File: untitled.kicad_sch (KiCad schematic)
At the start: 25 parts, among them U1 RP2040, X1 ASE-12.0MHz

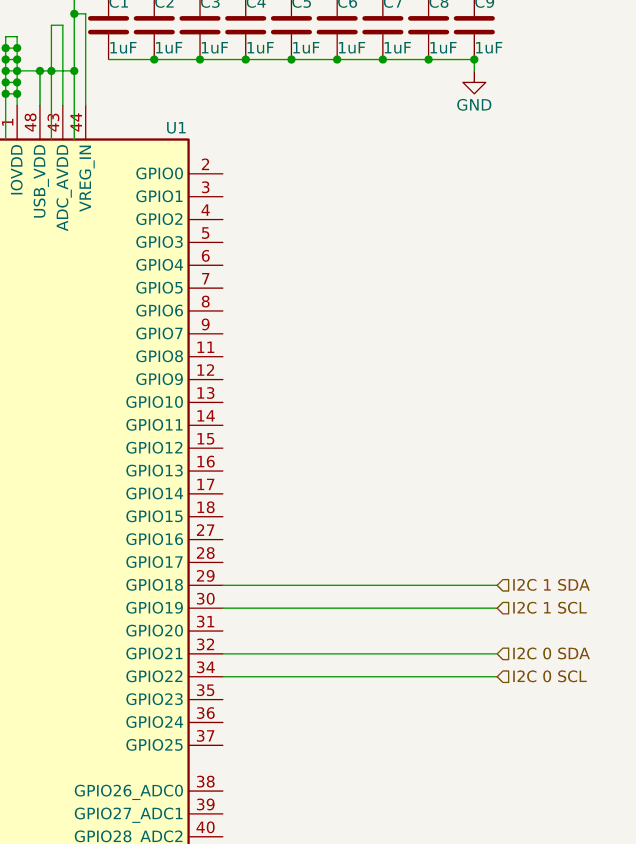
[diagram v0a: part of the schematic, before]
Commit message: exposes proper GPIO
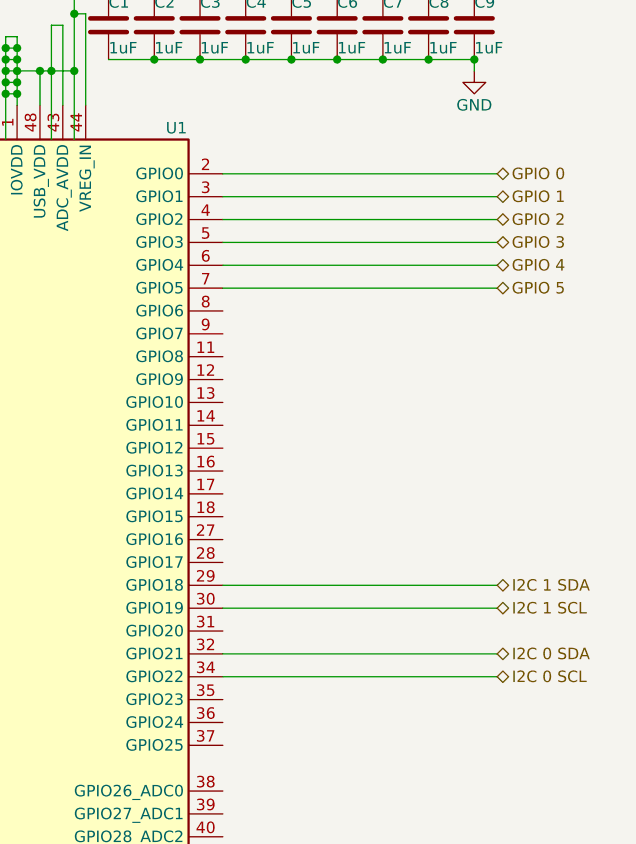
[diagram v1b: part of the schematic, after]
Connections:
- net GPIO 0: now reaches U1.2 (GPIO0)
- net GPIO 1: now reaches U1.3 (GPIO1)
- net GPIO 2: now reaches U1.4 (GPIO2)
- net GPIO 3: now reaches U1.5 (GPIO3)
- net GPIO 4: now reaches U1.6 (GPIO4)
- net GPIO 5: now reaches U1.7 (GPIO5)
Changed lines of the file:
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@@
+    (stroke (width 0) (type default))
+  )
+  (wire (pts (xy 143.51 52.07) (xy 173.99 52.07))
     (stroke (width 0) (type default))
   )
@@
     (stroke (width 0) (type default))
   )
+  (wire (pts (xy 143.51 46.99) (xy 173.99 46.99))
+    (stroke (width 0) (type default))
+  )
   (wire (pts (xy 125.73 34.29) (xy 125.73 25.4))
     (stroke (width 0) (type default))
@@
     (stroke (width 0) (type default))
   )
+  (wire (pts (xy 143.51 41.91) (xy 173.99 41.91))
+    (stroke (width 0) (type default))
+  )
   (wire (pts (xy 41.91 87.63) (xy 92.71 87.63))
     (stroke (width 0) (type default))
@@
     (stroke (width 0) (type default))
   )
+  (wire (pts (xy 143.51 49.53) (xy 173.99 49.53))
+    (stroke (width 0) (type default))
+  )
   (wire (pts (xy 120.65 30.48) (xy 120.65 29.21))
     (stroke (width 0) (type default))
@@
   )
   (wire (pts (xy 118.11 124.46) (xy 116.84 124.46))
+    (stroke (width 0) (type default))
+  )
+  (wire (pts (xy 143.51 54.61) (xy 173.99 54.61))
+    (stroke (width 0) (type default))
+  )
+  (wire (pts (xy 143.51 44.45) (xy 173.99 44.45))
     (stroke (width 0) (type default))
   )
@@
     (effects (font (size 1.27 1.27)) (justify left bottom))
   )
-  (hierarchical_label "I2C 1 SDA" (shape input) (at 173.99 87.63 0) (fields_autoplaced)
+  (hierarchical_label "I2C 1 SDA" (shape bidirectional) (at 173.99 87.63 0) (fields_autoplaced)
+    (effects (font (size 1.27 1.27)) (justify left))
+  )
+  (hierarchical_label "GPIO 5" (shape bidirectional) (at 173.99 54.61 0) (fields_autoplaced)
     (effects (font (size 1.27 1.27)) (justify left))
   )
@@
     (effects (font (size 1.27 1.27)) (justify right))
   )
+  (hierarchical_label "GPIO 4" (shape bidirectional) (at 173.99 52.07 0) (fields_autoplaced)
+    (effects (font (size 1.27 1.27)) (justify left))
+  )
   (hierarchical_label "USB_D-" (shape bidirectional) (at 74.93 49.53 180) (fields_autoplaced)
     (effects (font (size 1.27 1.27)) (justify right))
   )
+  (hierarchical_label "GPIO 2" (shape bidirectional) (at 173.99 46.99 0) (fields_autoplaced)
+    (effects (font (size 1.27 1.27)) (justify left))
+  )
+  (hierarchical_label "GPIO 0" (shape bidirectional) (at 173.99 41.91 0) (fields_autoplaced)
+    (effects (font (size 1.27 1.27)) (justify left))
+  )
   (hierarchical_label "QSPI_2" (shape bidirectional) (at 71.12 69.85 180) (fields_autoplaced)
     (effects (font (size 1.27 1.27)) (justify right))
@@
     (effects (font (size 1.27 1.27)) (justify left))
   )
-  (hierarchical_label "I2C 0 SDA" (shape input) (at 173.99 95.25 0) (fields_autoplaced)
+  (hierarchical_label "I2C 0 SDA" (shape bidirectional) (at 173.99 95.25 0) (fields_autoplaced)
     (effects (font (size 1.27 1.27)) (justify left))
   )
@@
     (effects (font (size 1.27 1.27)) (justify right))
   )
-  (hierarchical_label "I2C 0 SCL" (shape input) (at 173.99 97.79 0) (fields_autoplaced)
-    (effects (font (size 1.27 1.27)) (justify left))
-  )
-  (hierarchical_label "I2C 1 SCL" (shape input) (at 173.99 90.17 0) (fields_autoplaced)
-    (effects (font (size 1.27 1.27)) (justify left))
-  )
+  (hierarchical_label "I2C 0 SCL" (shape bidirectional) (at 173.99 97.79 0) (fields_autoplaced)
+    (effects (font (size 1.27 1.27)) (justify left))
+  )
+  (hierarchical_label "GPIO 3" (shape bidirectional) (at 173.99 49.53 0) (fields_autoplaced)
+    (effects (font (size 1.27 1.27)) (justify left))
+  )
+  (hierarchical_label "I2C 1 SCL" (shape bidirectional) (at 173.99 90.17 0) (fields_autoplaced)
+    (effects (font (size 1.27 1.27)) (justify left))
+  )
+  (hierarchical_label "GPIO 1" (shape bidirectional) (at 173.99 44.45 0) (fields_autoplaced)
+    (effects (font (size 1.27 1.27)) (justify left))
+  )
